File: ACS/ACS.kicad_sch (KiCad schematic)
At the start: 9 parts, among them Q1 IRLB8721PBF, U1 Teensy4.1, U2 TSR_1-2450, U3 BME280

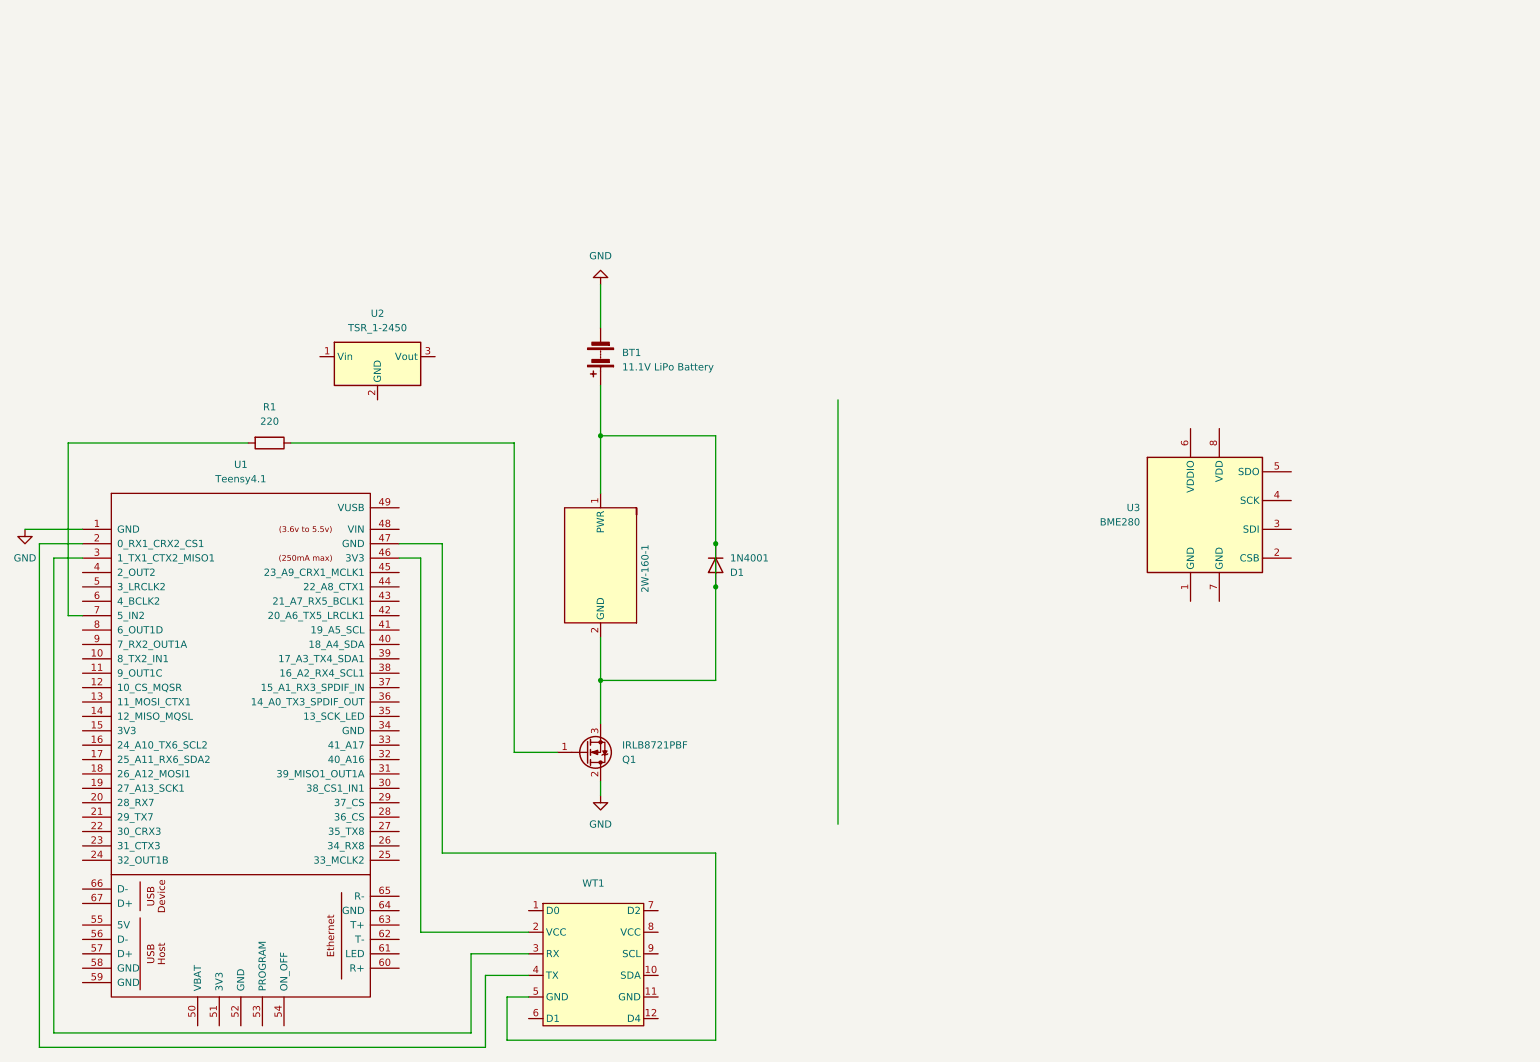
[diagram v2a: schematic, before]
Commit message: fixed all the wiring, added footprints for some, and cleaned up the schematic
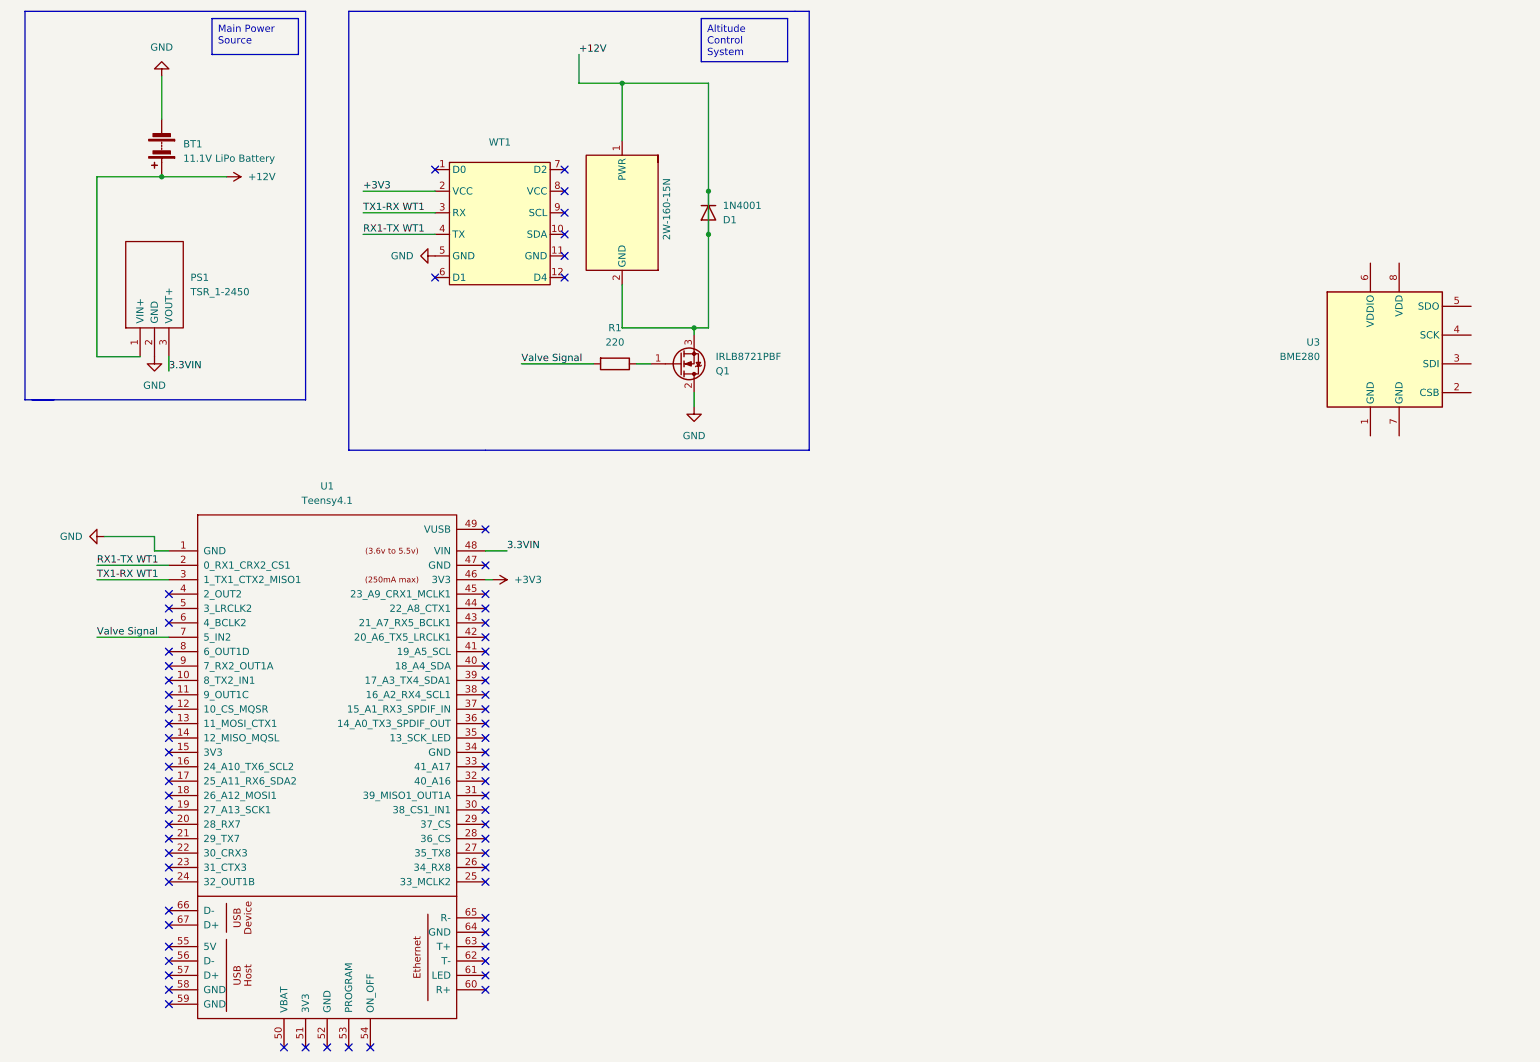
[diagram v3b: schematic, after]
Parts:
- removed U2: TSR_1-2450, Converter_DCDC:Converter_DCDC_TRACO_TSR-1_THT, symbol Regulator_Switching:TSR_1-2450
- added PS1: TSR_1-2450, random-footprints:TSR-1-24120, symbol random-symb-lib:TSR_1-2450
- U1: footprint (none) -> teensy-foots:Teensy41
- renumbered 2W-160-1 to 2W-160-15N
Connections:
- net GND: now also WT1.5 (GND), PS1.2 (GND)
- net +12V: now reaches 2W-160-15N.1 (PWR), 2W-160-15N.2 (GND), BT1.1 (+), D1.1 (K), D1.2 (A), Q1.3 (S)
- net +12V: now also PS1.1 (VIN+)
- net +3V3: now reaches U1.46 (3V3), WT1.2 (VCC)
- net TX1-RX WT1: now reaches U1.3 (1_TX1_CTX2_MISO1), WT1.3 (RX)
- net RX1-TX WT1: now reaches U1.2 (0_RX1_CRX2_CS1), WT1.4 (TX)
- net at U1.47 (GND): no longer WT1.5 (GND)
- net 3.3VIN: now reaches U1.48 (VIN)
- net 3.3VIN: now also PS1.3 (VOUT+)
- net Valve Signal: now reaches R1.2, U1.7 (5_IN2)
- no-connect marks 0 -> 69
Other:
- moved on the sheet: 2W-160-15N, BT1, D1, Q1, R1, U1, U3, WT1

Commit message: added all components, just need to add footprints
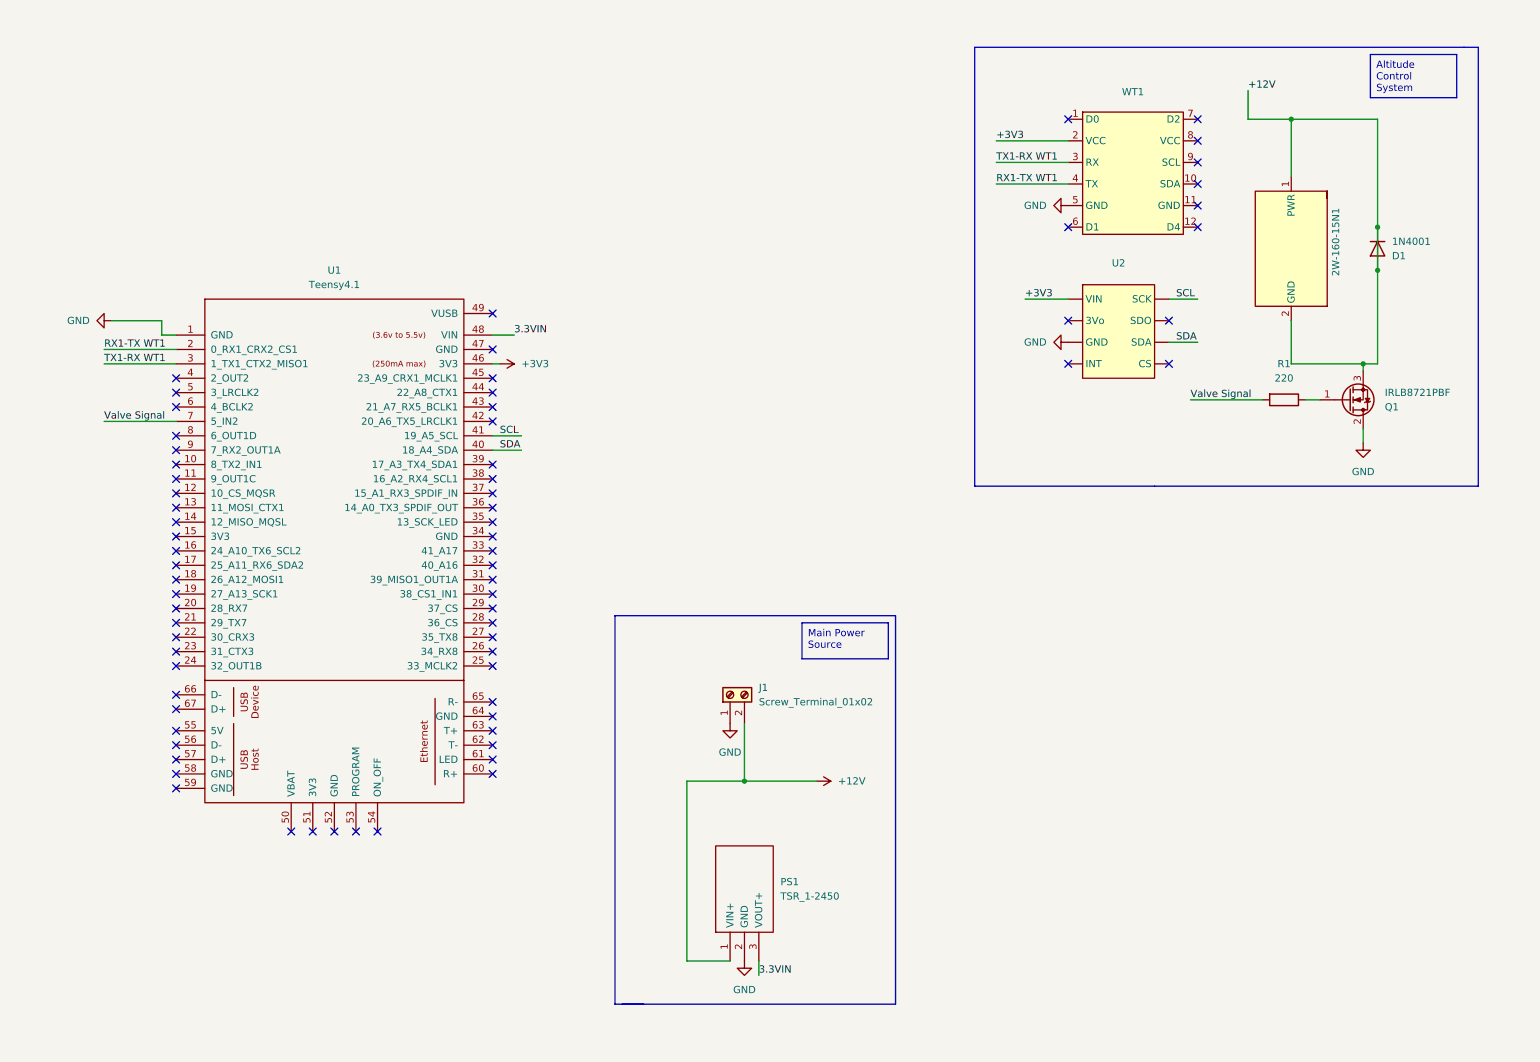
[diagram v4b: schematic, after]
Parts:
- removed BT1: 11.1V LiPo Battery, symbol Device:Battery
- removed U3: BME280, Package_LGA:Bosch_LGA-8_2.5x2.5mm_P0.65mm_ClockwisePinNumbering, symbol Sensor:BME280
- added J1: Screw_Terminal_01x02, TerminalBlock_RND:TerminalBlock_RND_205-00276_1x02_P5.00mm_Vertical, symbol Connector:Screw_Terminal_01x02
- added U2: ~, symbol random-symb-lib:ADA-BME388
- 2W-160-15N1: renamed from 2W-160-15N; footprint (none) -> TerminalBlock_RND:TerminalBlock_RND_205-00276_1x02_P5.00mm_Vertical
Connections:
- net +12V: now also J1.2 (Pin_2)
- net +3V3: now also U2. (VIN)
- net GND: now also J1.1 (Pin_1), U2. (VIN)
- net SDA: now reaches U1.40 (18_A4_SDA)
- net SDA: now also U2. (VIN)
- net SCL: now reaches U1.41 (19_A5_SCL)
- net SCL: now also U2. (VIN)
- no-connect marks 69 -> 71
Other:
- moved on the sheet: 2W-160-15N1, D1, PS1, Q1, R1, U1, WT1

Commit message: Sunday Update
integrated BMP388, WT901 and Solenoid. Update Schematic and add example code to test all component
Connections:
- net +3V3: now also WT1.8 (VCC); no longer WT1.2 (VCC)
- net GND: now also WT1.11 (GND); no longer WT1.5 (GND)
- net SCL: now also WT1.9 (SCL)
- net SDA: now also WT1.10 (SDA)
- net RX1-TX WT1: no longer names the net of WT1.4 (TX)
- net RX1-TX WT1: no longer U1.2 (0_RX1_CRX2_CS1)
- net TX1-RX WT1: no longer names the net of WT1.3 (RX)
- net TX1-RX WT1: no longer U1.3 (1_TX1_CTX2_MISO1)
- no-connect marks 71 -> 73
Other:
- moved on the sheet: WT1
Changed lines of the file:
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@@
+	)
+	(no_connect
+		(at 191.77 44.45)
 	)
 	(no_connect
@@
 	)
 	(no_connect
+		(at 40.64 76.2)
+	)
+	(no_connect
 		(at 215.9 68.58)
 	)
 	(no_connect
-		(at 198.12 52.07)
+		(at 191.77 52.07)
 	)
 	(no_connect
@@
 	)
 	(no_connect
-		(at 198.12 33.02)
+		(at 191.77 33.02)
 	)
 	(no_connect
@@
 	)
 	(no_connect
+		(at 191.77 48.26)
+	)
+	(no_connect
 		(at 40.64 99.06)
 	)
@@
 	)
 	(no_connect
-		(at 220.98 52.07)
-	)
-	(no_connect
-		(at 220.98 36.83)
+		(at 214.63 52.07)
 	)
 	(no_connect
@@
 	)
 	(no_connect
-		(at 220.98 40.64)
-	)
-	(no_connect
 		(at 96.52 81.28)
 	)
@@
 	)
 	(no_connect
-		(at 220.98 33.02)
+		(at 214.63 33.02)
 	)
 	(no_connect
@@
 	)
 	(no_connect
-		(at 220.98 48.26)
-	)
-	(no_connect
 		(at 96.52 121.92)
 	)
 	(no_connect
-		(at 220.98 44.45)
+		(at 191.77 36.83)
 	)
 	(no_connect
@@
 	)
 	(no_connect
+		(at 191.77 40.64)
+	)
+	(no_connect
 		(at 96.52 119.38)
 	)
@@
 	)
 	(no_connect
+		(at 40.64 73.66)
+	)
+	(no_connect
 		(at 40.64 143.51)
 	)
@@
 	(wire
 		(pts
-			(xy 27.94 76.2) (xy 40.64 76.2)
-		)
-		(stroke
-			(width 0)
-			(type default)
-		)
-	)
-	(wire
-		(pts
-			(xy 185.42 44.45) (xy 198.12 44.45)
-		)
-		(stroke
-			(width 0)
-			(type default)
-		)
-	)
-	(wire
-		(pts
 			(xy 229.87 27.94) (xy 229.87 33.02)
 		)
@@
 		)
 	)
+	(wire
+		(pts
+			(xy 214.63 40.64) (xy 219.71 40.64)
+		)
+		(stroke
+			(width 0)
+			(type default)
+		)
+	)
 	(polyline
 		(pts
@@
 	(wire
 		(pts
+			(xy 214.63 48.26) (xy 217.17 48.26)
+		)
+		(stroke
+			(width 0)
+			(type default)
+		)
+	)
+	(wire
+		(pts
 			(xy 143.51 181.61) (xy 143.51 184.15)
 		)
@@
 	(wire
 		(pts
-			(xy 27.94 73.66) (xy 40.64 73.66)
-		)
-		(stroke
-			(width 0)
-			(type default)
-		)
-	)
-	(wire
-		(pts
 			(xy 29.21 68.58) (xy 38.1 68.58)
 		)
@@
 	(wire
 		(pts
+			(xy 219.71 36.83) (xy 214.63 36.83)
+		)
+		(stroke
+			(width 0)
+			(type default)
+		)
+	)
+	(wire
+		(pts
 			(xy 237.49 33.02) (xy 237.49 43.18)
 		)
@@
 	(wire
 		(pts
-			(xy 185.42 36.83) (xy 198.12 36.83)
-		)
-		(stroke
-			(width 0)
-			(type default)
-		)
-	)
-	(wire
-		(pts
 			(xy 97.79 76.2) (xy 96.52 76.2)
 		)
@@
 	(wire
 		(pts
+			(xy 214.63 44.45) (xy 219.71 44.45)
+		)
+		(stroke
+			(width 0)
+			(type default)
+		)
+	)
+	(wire
+		(pts
 			(xy 96.52 71.12) (xy 100.33 71.12)
 		)
@@
 		(pts
 			(xy 250.19 76.2) (xy 250.19 77.47)
-		)
-		(stroke
-			(width 0)
-			(type default)
-		)
-	)
-	(wire
-		(pts
-			(xy 198.12 40.64) (xy 185.42 40.64)
 		)
 		(stroke
@@
 		)
 	)
-	(label "RX1-TX WT1"
-		(at 27.94 73.66 0)
+	(label "SCL"
+		(at 215.9 40.64 0)
 		(fields_autoplaced yes)
 		(effects
@@
 		)
 	)
-	(label "TX1-RX WT1"
-		(at 27.94 76.2 0)
+	(label "+12V"
+		(at 229.87 27.94 0)
 		(fields_autoplaced yes)
 		(effects
@@
 		)
 	)
-	(label "+12V"
-		(at 229.87 27.94 0)
+	(label "SDA"
+		(at 217.17 72.39 0)
 		(fields_autoplaced yes)
 		(effects
@@
 	)
 	(label "+3V3"
-		(at 185.42 36.83 0)
+		(at 190.5 64.77 0)
 		(fields_autoplaced yes)
 		(effects
@@
 		)
 	)
-	(label "SDA"
-		(at 217.17 72.39 0)
+	(label "+3V3"
+		(at 214.63 36.83 0)
 		(fields_autoplaced yes)
 		(effects
@@
 		)
 	)
-	(label "+3V3"
-		(at 190.5 64.77 0)
+	(label "SCL"
+		(at 97.79 88.9 0)
 		(fields_autoplaced yes)
 		(effects
@@
 		)
 	)
-	(label "SCL"
-		(at 97.79 88.9 0)
+	(label "3.3VIN"
+		(at 100.33 71.12 0)
 		(fields_autoplaced yes)
 		(effects
@@
 		)
 	)
-	(label "3.3VIN"
-		(at 100.33 71.12 0)
-		(fields_autoplaced yes)
-		(effects
-			(font
-				(size 1.27 1.27)
-			)
-			(justify left bottom)
-		)
-	)
-	(label "RX1-TX WT1"
-		(at 185.42 44.45 0)
-		(fields_autoplaced yes)
-		(effects
-			(font
-				(size 1.27 1.27)
-			)
-			(justify left bottom)
-		)
-	)
-	(label "TX1-RX WT1"
-		(at 185.42 40.64 0)
+	(label "SDA"
+		(at 215.9 44.45 0)
 		(fields_autoplaced yes)
 		(effects
@@
 	(symbol
 		(lib_id "grs_comps:WT901")
-		(at 209.55 41.91 0)
+		(at 203.2 41.91 0)
 		(unit 1)
 		(exclude_from_sim no)
@@
 		(fields_autoplaced yes)
 		(property "Reference" "WT1"
-			(at 209.55 28.194 0)
+			(at 203.2 28.194 0)
 			(effects
 				(font
@@
 		)
 		(property "Value" "~"
-			(at 209.55 30.734 0)
+			(at 203.2 30.734 0)
 			(effects
 				(font
@@
 		)
 		(property "Footprint" ""
-			(at 209.55 41.91 0)
+			(at 203.2 41.91 0)
 			(effects
 				(font
@@
 		)
 		(property "Datasheet" ""
-			(at 209.55 41.91 0)
+			(at 203.2 41.91 0)
 			(effects
 				(font
@@
 		)
 		(property "Description" ""
-			(at 209.55 41.91 0)
+			(at 203.2 41.91 0)
 			(effects
 				(font
@@
 	(symbol
 		(lib_id "power:GND")
-		(at 198.12 48.26 270)
+		(at 217.17 48.26 90)
+		(mirror x)
 		(unit 1)
 		(exclude_from_sim no)
@@
 		(on_board yes)
 		(dnp no)
-		(fields_autoplaced yes)
 		(property "Reference" "#PWR05"
-			(at 191.77 48.26 0)
+			(at 223.52 48.26 0)
 			(effects
 				(font
@@
 		)
 		(property "Value" "GND"
-			(at 194.31 48.2599 90)
+			(at 220.726 48.26 90)
 			(effects
 				(font
@@
 		)
 		(property "Footprint" ""
-			(at 198.12 48.26 0)
+			(at 217.17 48.26 0)
 			(effects
 				(font
@@
 		)
 		(property "Datasheet" ""
-			(at 198.12 48.26 0)
+			(at 217.17 48.26 0)
 			(effects
 				(font
@@
 		)
 		(property "Description" "Power symbol creates a global label with name \"GND\" , ground"
-			(at 198.12 48.26 0)
-			(effects
-				(font
+			(at 217.17 48.26 0)
+			(effects
+				(font
